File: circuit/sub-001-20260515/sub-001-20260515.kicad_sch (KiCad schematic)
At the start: 148 parts, among them J1 Conn_NeoPixel, J2 Conn_SW_TGL, J3 Conn_Power, J4 Conn_Main, Q1 BSS138, Q2 BSS138, Q3 BSS138, Q4 BSS138, Q5 BSS138, Q6 BSS138, Q7 BSS138, Q8 BSS138, U11 LM1117GS-3.3, U12 NE555DR, U13 NE555DR, U14 LM1117GS-3.3, U15 LM1117GS-3.3, U18 NE555DR, U19 NE555DR, U2 LM1117GS-3.3, U20 TSSP58038, U21 TSSP58038, U22 NE555DR, U23 NE555DR, U24 TSSP58038, U25 TSSP58038, U26 HC-SR04, U27 HC-SR04, U28 HC-SR04, U29 HC-SR04, U4 NE555DR, U5 NE555DR, U7 LM1117GS-3.3, U9 LM1117MP-3.3

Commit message: Update サブ基板のPCBを進めた
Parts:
- R47, R48, R49: footprint (none) -> Resistor_SMD:R_0805_2012Metric
- U16, U17: footprint (none) -> @Thrive_footprint_sub:XIAO-ESP32-C3-DIP
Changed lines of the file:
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@@
 			)
 		)
-		(property "Footprint" ""
+		(property "Footprint" "Resistor_SMD:R_0805_2012Metric"
 			(at 376.682 179.07 90)
 			(hide yes)
@@
 			)
 		)
-		(property "Footprint" ""
+		(property "Footprint" "@Thrive_footprint_sub:XIAO-ESP32-C3-DIP"
 			(at 210.82 54.102 0)
 			(hide yes)
@@
 			)
 		)
-		(property "Footprint" ""
+		(property "Footprint" "@Thrive_footprint_sub:XIAO-ESP32-C3-DIP"
 			(at 210.82 18.542 0)
 			(hide yes)
@@
 			)
 		)
-		(property "Footprint" ""
+		(property "Footprint" "Resistor_SMD:R_0805_2012Metric"
 			(at 367.792 179.07 90)
 			(hide yes)
@@
 			)
 		)
-		(property "Footprint" ""
+		(property "Footprint" "Resistor_SMD:R_0805_2012Metric"
 			(at 385.572 179.07 90)
 			(hide yes)

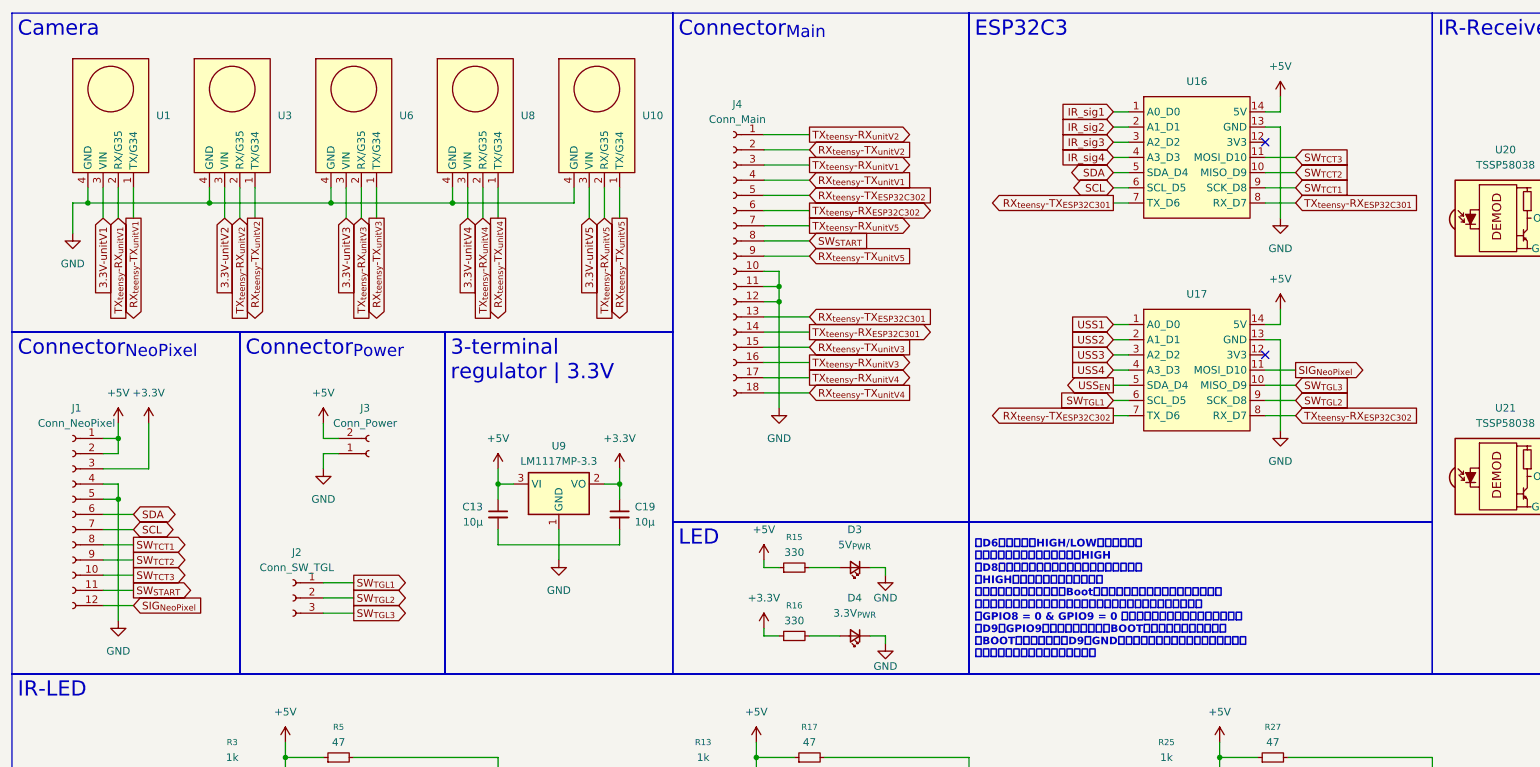
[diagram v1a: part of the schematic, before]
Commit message: Update サブ基板のFPCコネクタ周りを更新
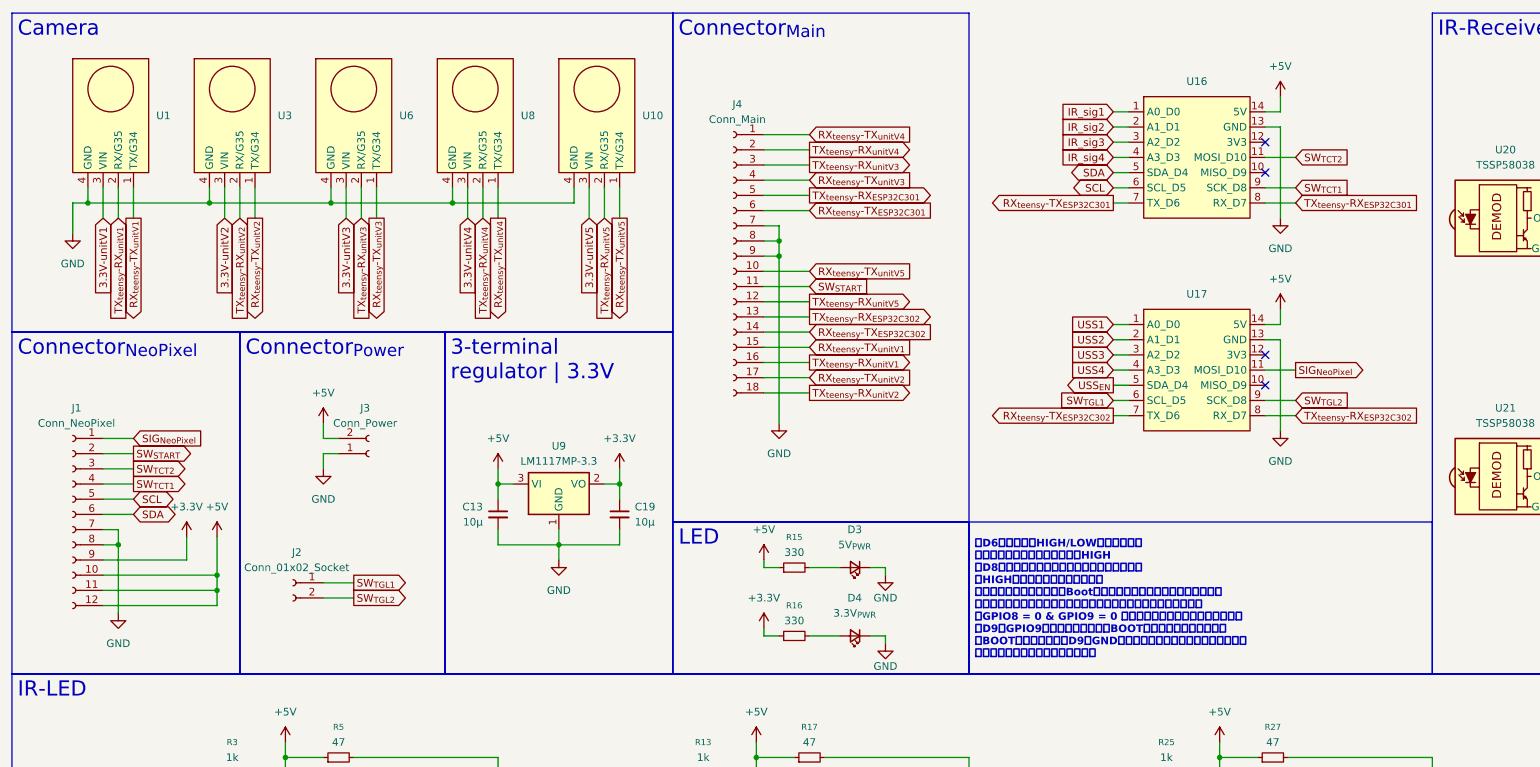
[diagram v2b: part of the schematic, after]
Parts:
- removed J2: Conn_SW_TGL, Connector_PinSocket_2.54mm:PinSocket_1x03_P2.54mm_Vertical, symbol Connector:Conn_01x03_Socket
- added J2: Conn_01x02_Socket, symbol Connector:Conn_01x02_Socket
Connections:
- net +3.3V: now also J1.9 (Pin_9); no longer J1.3 (Pin_3)
- net +5V: now also J1.10 (Pin_10), J1.11 (Pin_11), J1.12 (Pin_12); no longer J1.1 (Pin_1), J1.2 (Pin_2)
- net GND: now also C13.2, C19.2, J1.7 (Pin_7), J1.8 (Pin_8), J4.7 (Pin_7), J4.8 (Pin_8), J4.9 (Pin_9); no longer J1.4 (Pin_4), J1.5 (Pin_5), J4.10 (Pin_10), J4.11 (Pin_11), J4.12 (Pin_12)
- net RX_{teensy}-TX_{ESP32C301}: now also J4.6 (Pin_6); no longer J4.13 (Pin_13)
- net RX_{teensy}-TX_{ESP32C302}: now also J4.14 (Pin_14); no longer J4.5 (Pin_5)
- net RX_{teensy}-TX_{unitV1}: now also J4.15 (Pin_15); no longer J4.4 (Pin_4)
- net RX_{teensy}-TX_{unitV2}: now also J4.17 (Pin_17); no longer J4.2 (Pin_2)
- net RX_{teensy}-TX_{unitV3}: now also J4.4 (Pin_4); no longer J4.15 (Pin_15)
- net RX_{teensy}-TX_{unitV4}: now also J4.1 (Pin_1); no longer J4.18 (Pin_18)
- net RX_{teensy}-TX_{unitV5}: now also J4.10 (Pin_10); no longer J4.9 (Pin_9)
- net SCL: now also J1.5 (Pin_5); no longer J1.7 (Pin_7)
- net SIG_{NeoPixel}: now also J1.1 (Pin_1); no longer J1.12 (Pin_12)
- net SW_{START}: now also J1.2 (Pin_2), J4.11 (Pin_11); no longer J1.11 (Pin_11), J4.8 (Pin_8)
- net SW_{TCT1}: now also J1.4 (Pin_4); no longer J1.8 (Pin_8)
- net SW_{TCT2}: now also J1.3 (Pin_3), U16.11 (MOSI_D10); no longer J1.9 (Pin_9), U16.10 (MISO_D9)
- net SW_{TGL1}: now also J2.1 (Pin_1)
- net SW_{TGL2}: now also J2.2 (Pin_2)
- net SW_{TGL3}: no longer U17.10 (MISO_D9)
- net TX_{teensy}-RX_{ESP32C301}: now also J4.5 (Pin_5); no longer J4.14 (Pin_14)
- net TX_{teensy}-RX_{ESP32C302}: now also J4.13 (Pin_13); no longer J4.6 (Pin_6)
- net TX_{teensy}-RX_{unitV1}: now also J4.16 (Pin_16); no longer J4.3 (Pin_3)
- net TX_{teensy}-RX_{unitV2}: now also J4.18 (Pin_18); no longer J4.1 (Pin_1)
- net TX_{teensy}-RX_{unitV3}: now also J4.3 (Pin_3); no longer J4.16 (Pin_16)
- net TX_{teensy}-RX_{unitV4}: now also J4.2 (Pin_2); no longer J4.17 (Pin_17)
- net TX_{teensy}-RX_{unitV5}: now also J4.12 (Pin_12); no longer J4.7 (Pin_7)
- removed net SW_{TCT3}: J1.10 (Pin_10), U16.11 (MOSI_D10)
- no-connect marks 2 -> 4
